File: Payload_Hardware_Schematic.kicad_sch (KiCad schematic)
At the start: 11 parts, among them J1 Micro_SD_Card, J2 Conn_01x06_Pin_5V, J3 Conn_01x06_Pin_3V3, J4 Conn_01x04_Pin, J5 Conn_01x08_Pin, U1 STM32F411 BlackPill, U2 MPM3610, U3 BMP388, U4 LSM9DS1, U5 MPM3610

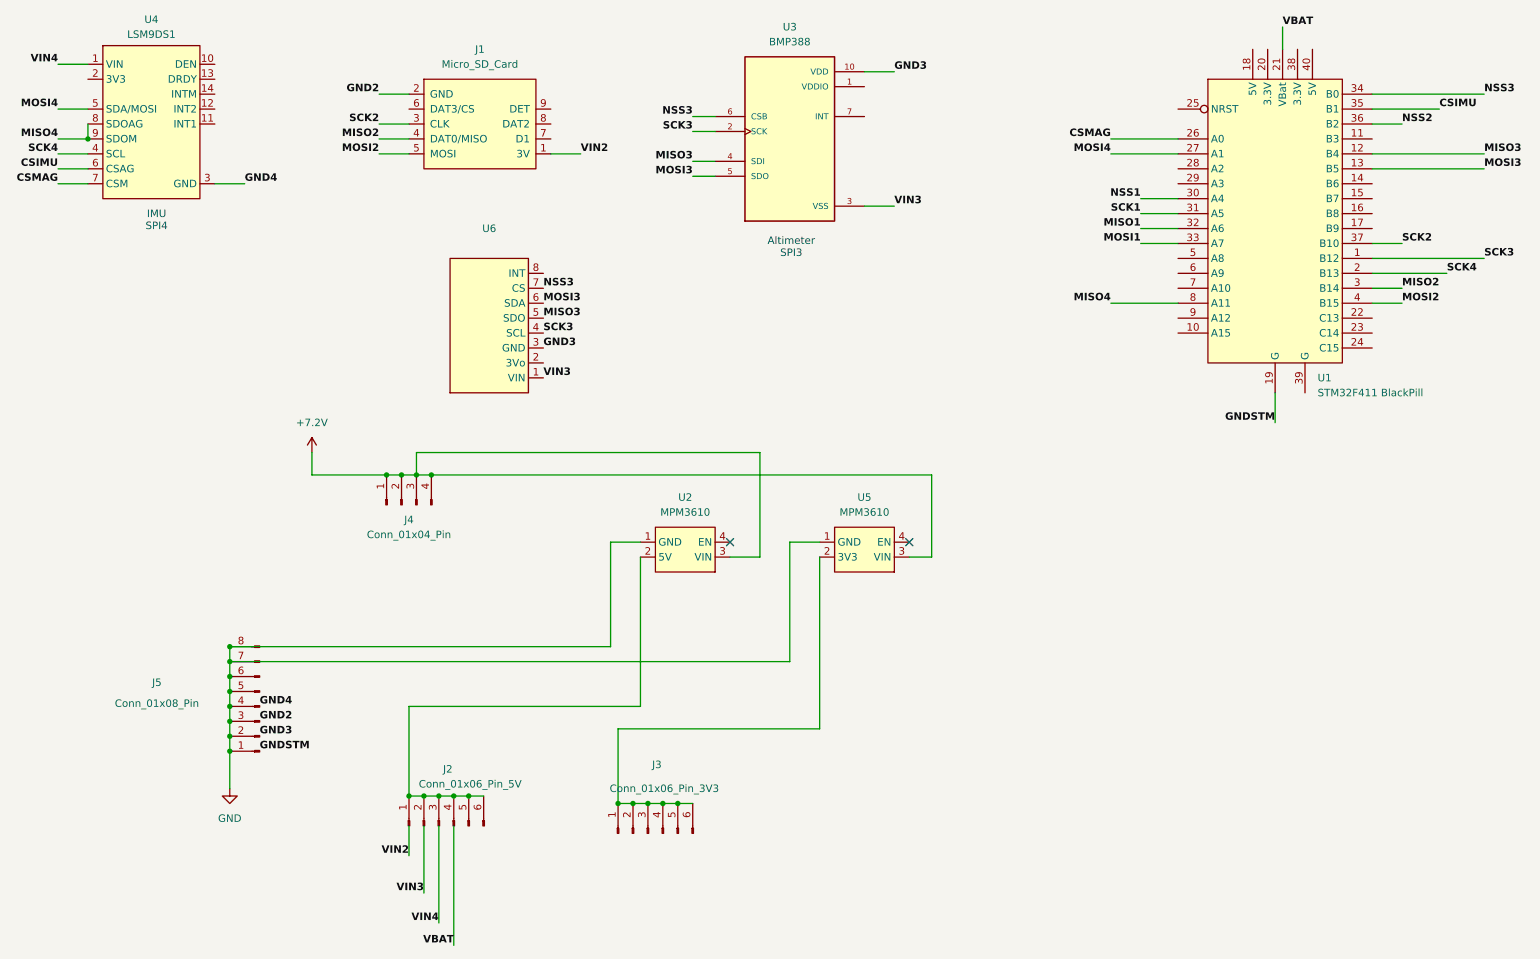
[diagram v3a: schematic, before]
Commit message: Fixed footprints and schematics
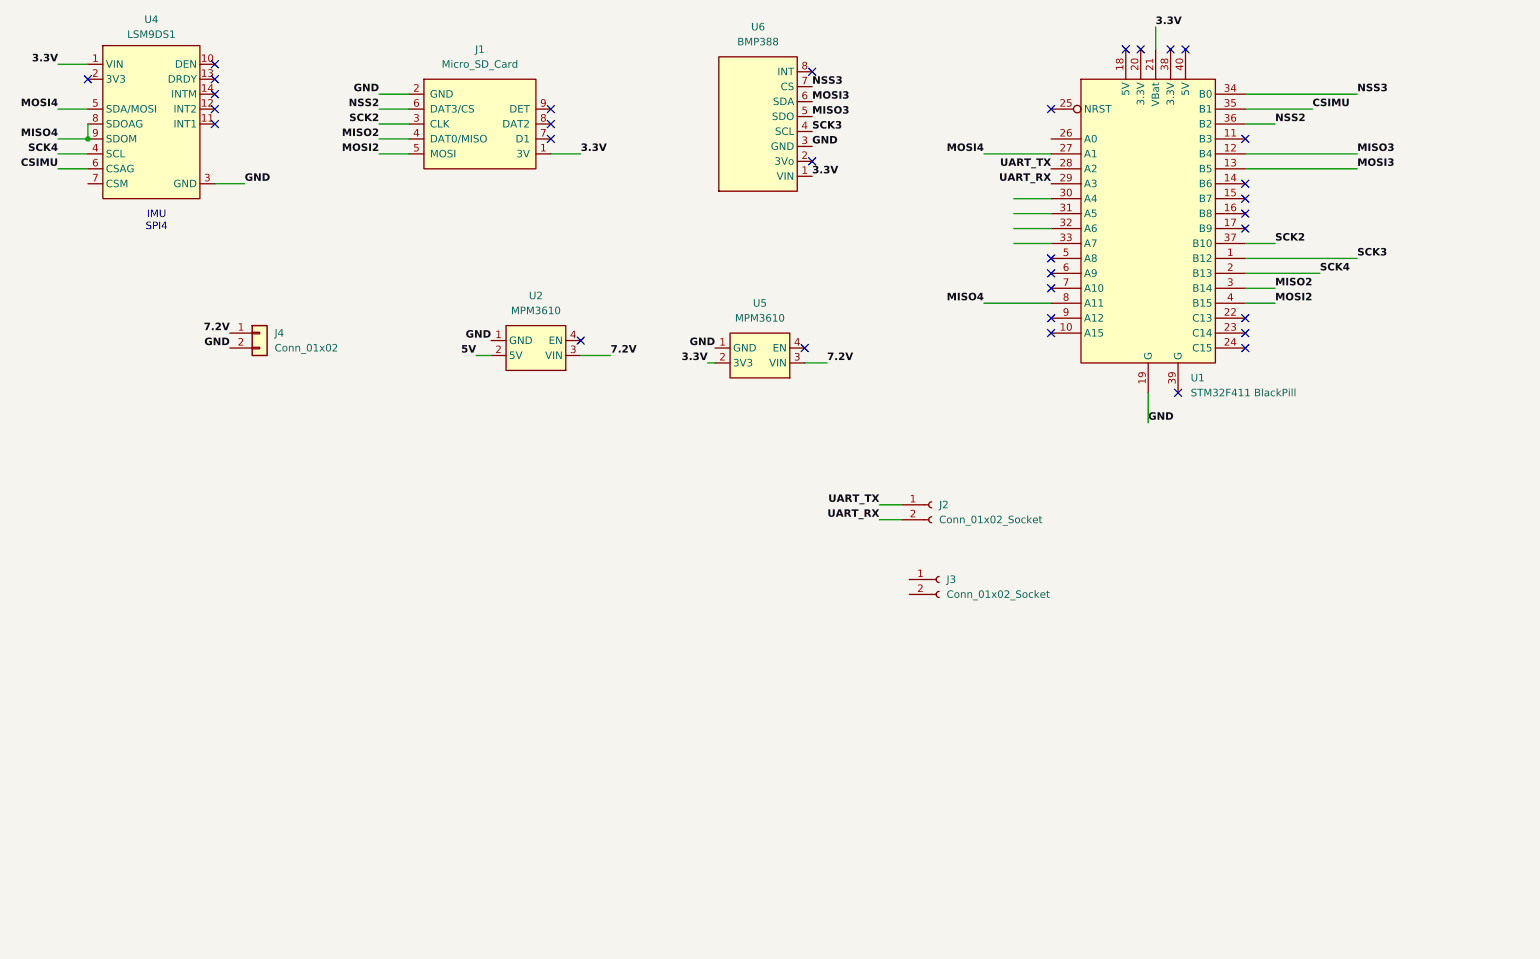
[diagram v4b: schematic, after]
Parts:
- removed J2: Conn_01x06_Pin_5V, Connector_PinSocket_2.54mm:PinSocket_1x06_P2.54mm_Vertical, symbol Connector:Conn_01x06_Pin
- removed J3: Conn_01x06_Pin_3V3, Connector_PinSocket_2.54mm:PinSocket_1x06_P2.54mm_Vertical, symbol Connector:Conn_01x06_Pin
- removed J4: Conn_01x04_Pin, Connector_PinSocket_2.54mm:PinSocket_1x04_P2.54mm_Vertical, symbol Connector:Conn_01x04_Pin
- removed J5: Conn_01x08_Pin, Connector_PinSocket_2.54mm:PinSocket_1x08_P2.54mm_Vertical, symbol Connector:Conn_01x08_Pin
- removed U3: BMP388, BMP388:BMP388_Breakout, symbol BMP388:BMP388
- added J2, J3: Conn_01x02_Socket, symbol Connector:Conn_01x02_Socket
- added J4: Conn_01x02, symbol Connector_Generic:Conn_01x02
- U6: value ~ -> BMP388
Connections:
- net GND3 is gone; now on net GND: U6.3 (GND)
- net GND4 is gone; now on net GND: U4.3 (GND)
- net GNDSTM is gone; now on net GND: U1.19 (G)
- net VBAT is gone; now on net GND: U1.21 (VBat)
- net VIN4 is gone; now on net GND: U4.1 (VIN)
- net VSS is gone; now on net GND: U6.1 (VIN)
- net GND: now also J1.2 (GND), U5.2 (3V3), J4.2 (Pin_2)
- net NSS2: now also J1.6 (DAT3/CS)
- net 5V: now reaches U2.2 (5V)
- net UART_TX: now reaches U1.28 (A2)
- net UART_TX: now also J2.1 (Pin_1)
- net UART_RX: now reaches U1.29 (A3)
- net UART_RX: now also J2.2 (Pin_2)
- net +7.2V renamed 7.2V
- net 7.2V: now also J4.1 (Pin_1)
- net CSMAG: no longer names the net of U4.7 (CSM)
- net CSMAG: no longer U1.26 (A0)
- net MISO1: no longer names the net of U1.32 (A6)
- net MOSI1: no longer names the net of U1.33 (A7)
- net NSS1: no longer names the net of U1.30 (A4)
- net SCK1: no longer names the net of U1.31 (A5)
- no-connect marks 2 -> 32
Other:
- note removed: "Altimeter SPI3"
- moved on the sheet: U1, U2, U5, U6

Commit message: updated footprints
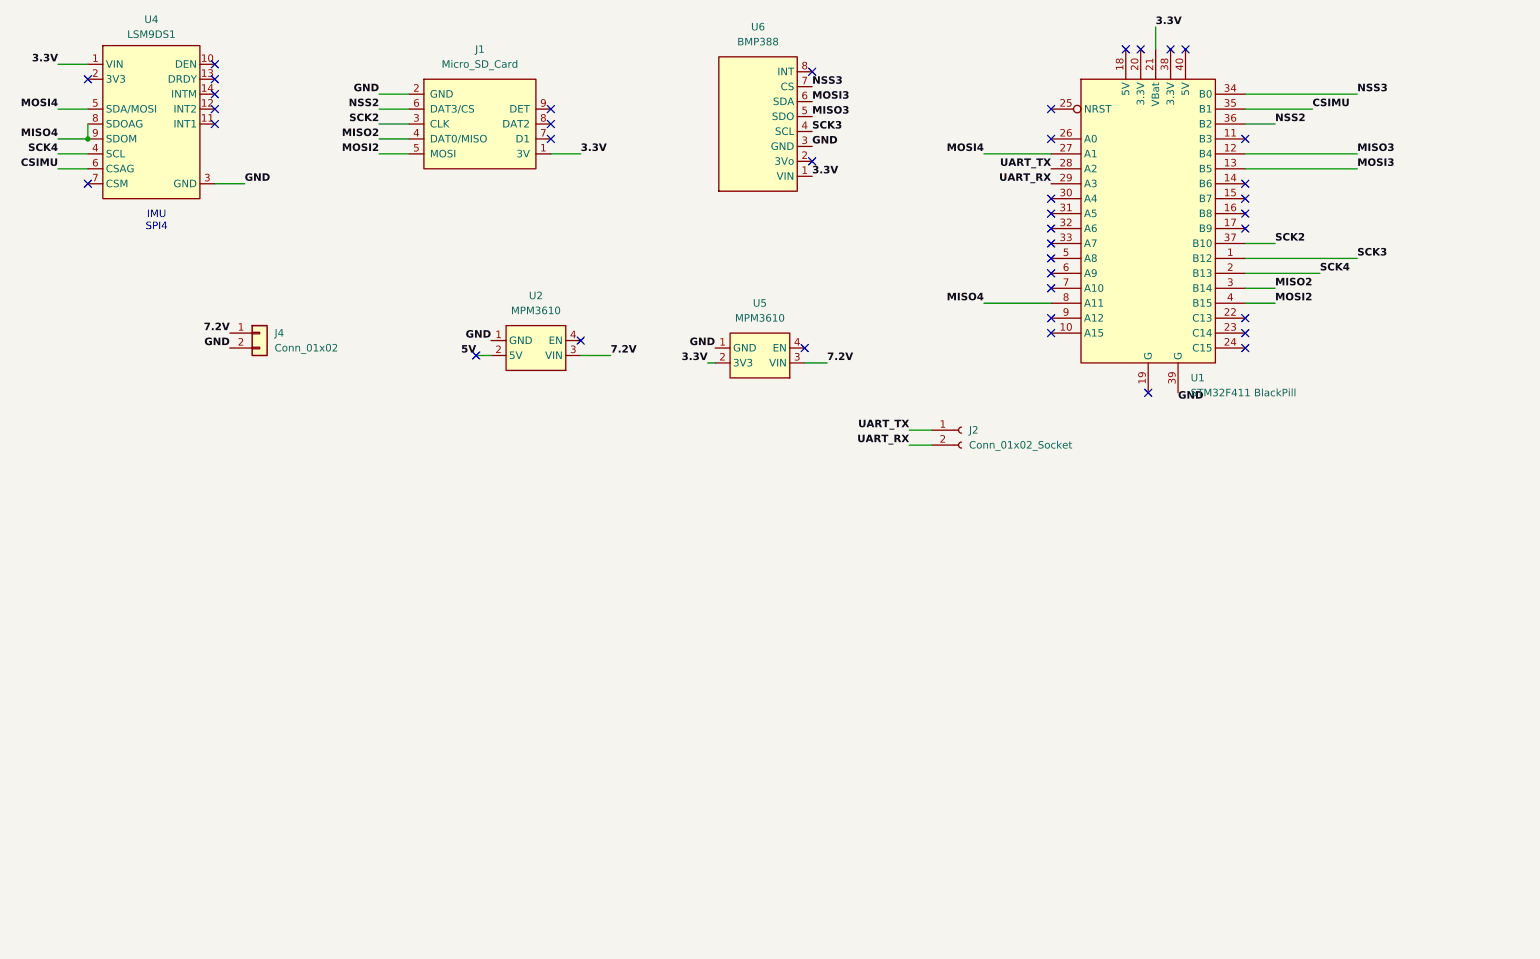
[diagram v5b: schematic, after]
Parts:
- removed J3: Conn_01x02_Socket, symbol Connector:Conn_01x02_Socket
- J2: footprint (none) -> Connector_PinSocket_2.54mm:PinSocket_1x02_P2.54mm_Vertical
- J4: footprint (none) -> Microfit-Header:CONN_SD-43650-001_02_MOL
- U2, U5: footprint PowerRegulation:MPM3610 -> PowerRugulators:MPM3610
- U6: footprint BMP388:BMP388_Breakout -> Payload-BMP388:BMP388_Breakout
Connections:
- net GND: now also U1.39 (G); no longer U1.19 (G)
- no-connect marks 32 -> 39
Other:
- moved on the sheet: J2
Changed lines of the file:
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@@
+	)
+	(no_connect
+		(at 34.29 46.99)
 	)
 	(no_connect
@@
 	)
 	(no_connect
-		(at 219.71 82.55)
+		(at 198.12 39.37)
+	)
+	(no_connect
+		(at 214.63 82.55)
 	)
 	(no_connect
@@
 	)
 	(no_connect
+		(at 198.12 57.15)
+	)
+	(no_connect
 		(at 198.12 59.69)
 	)
@@
 	)
 	(no_connect
+		(at 198.12 52.07)
+	)
+	(no_connect
 		(at 55.88 29.21)
 	)
@@
 	)
 	(no_connect
+		(at 198.12 49.53)
+	)
+	(no_connect
+		(at 198.12 54.61)
+	)
+	(no_connect
 		(at 156.21 74.93)
 	)
@@
 	)
 	(no_connect
+		(at 100.33 76.2)
+	)
+	(no_connect
 		(at 231.14 54.61)
 	)
@@
 	(wire
 		(pts
-			(xy 168.91 101.6) (xy 172.72 101.6)
-		)
-		(stroke
-			(width 0)
-			(type default)
-		)
-	)
-	(wire
-		(pts
-			(xy 191.77 57.15) (xy 198.12 57.15)
+			(xy 173.99 88.9) (xy 177.8 88.9)
 		)
 		(stroke
@@
 	(wire
 		(pts
-			(xy 191.77 52.07) (xy 198.12 52.07)
-		)
-		(stroke
-			(width 0)
-			(type default)
-		)
-	)
-	(wire
-		(pts
 			(xy 231.14 36.83) (xy 236.22 36.83)
 		)
@@
 	(wire
 		(pts
-			(xy 191.77 54.61) (xy 198.12 54.61)
-		)
-		(stroke
-			(width 0)
-			(type default)
-		)
-	)
-	(wire
-		(pts
 			(xy 29.21 39.37) (xy 34.29 39.37)
 		)
@@
 	(wire
 		(pts
-			(xy 214.63 82.55) (xy 214.63 87.63)
-		)
-		(stroke
-			(width 0)
-			(type default)
-		)
-	)
-	(wire
-		(pts
 			(xy 83.82 31.75) (xy 88.9 31.75)
 		)
@@
 	(wire
 		(pts
-			(xy 191.77 49.53) (xy 198.12 49.53)
-		)
-		(stroke
-			(width 0)
-			(type default)
-		)
-	)
-	(wire
-		(pts
 			(xy 231.14 41.91) (xy 250.19 41.91)
 		)
@@
 	(wire
 		(pts
-			(xy 168.91 104.14) (xy 172.72 104.14)
+			(xy 173.99 91.44) (xy 177.8 91.44)
 		)
 		(stroke
@@
 	)
 	(label "GND"
-		(at 214.63 87.63 0)
-		(effects
-			(font
-				(size 1.27 1.27)
-				(thickness 0.254)
-				(bold yes)
-			)
-			(justify left bottom)
+		(at 219.71 82.55 0)
+		(effects
+			(font
+				(size 1.27 1.27)
+				(thickness 0.254)
+				(bold yes)
+			)
+			(justify top)
 		)
 	)
@@
 	)
 	(label "UART_RX"
-		(at 168.91 104.14 180)
+		(at 173.99 91.44 180)
 		(effects
 			(font
@@
 	)
 	(label "UART_TX"
-		(at 168.91 101.6 180)
+		(at 173.99 88.9 180)
 		(effects
 			(font
@@
 			)
 			(justify left bottom)
-		)
-	)
-	(symbol
-		(lib_id "Connector:Conn_01x02_Socket")
-		(at 179.07 114.3 0)
-		(unit 1)
-		(exclude_from_sim no)
-		(in_bom yes)
-		(on_board yes)
-		(dnp no)
-		(fields_autoplaced yes)
-		(property "Reference" "J3"
-			(at 180.34 114.2999 0)
-			(effects
-				(font
-					(size 1.27 1.27)
-				)
-				(justify left)
-			)
-		)
-		(property "Value" "Conn_01x02_Socket"
-			(at 180.34 116.8399 0)
-			(effects
-				(font
-					(size 1.27 1.27)
-				)
-				(justify left)
-			)
-		)
-		(property "Footprint" ""
-			(at 179.07 114.3 0)
-			(effects
-				(font
-					(size 1.27 1.27)
-				)
-				(hide yes)
-			)
-		)
-		(property "Datasheet" "~"
-			(at 179.07 114.3 0)
-			(effects
-				(font
-					(size 1.27 1.27)
-				)
-				(hide yes)
-			)
-		)
-		(property "Description" "Generic connector, single row, 01x02, script generated"
-			(at 179.07 114.3 0)
-			(effects
-				(font
-					(size 1.27 1.27)
-				)
-				(hide yes)
-			)
-		)
-		(pin "2"
-		)
-		(pin "1"
-		)
-		(instances
-			(project "Payload_Hardware_Schematic"
-				(path "/f4ead8bb-2437-4e54-a6d9-f5ca11bfd675"
-					(reference "J3")
-					(unit 1)
-				)
-			)
 		)
 	)
@@
 			)
 		)
-		(property "Footprint" "BMP388:BMP388_Breakout"
+		(property "Footprint" "Payload-BMP388:BMP388_Breakout"
 			(at 151.13 34.29 0)
 			(effects
@@
 			)
 		)
-		(property "Footprint" ""
+		(property "Footprint" "Microfit-Header:CONN_SD-43650-001_02_MOL"
 			(at 63.5 72.39 0)
 			(effects
@@
 			)
 		)
-		(property "Footprint" "PowerRegulation:MPM3610"
+		(property "Footprint" "PowerRugulators:MPM3610"
 			(at 147.32 69.85 0)
 			(effects
@@
 			)
 		)
-		(property "Footprint" "PowerRegulation:MPM3610"
+		(property "Footprint" "PowerRugulators:MPM3610"
 			(at 109.22 68.58 0)
 			(effects
@@
 	(symbol
 		(lib_id "Connector:Conn_01x02_Socket")
-		(at 177.8 101.6 0)
+		(at 182.88 88.9 0)
 		(unit 1)
 		(exclude_from_sim no)
@@
 		(fields_autoplaced yes)
 		(property "Reference" "J2"
-			(at 179.07 101.5999 0)
+			(at 184.15 88.8999 0)
 			(effects
 				(font
@@
 		)
 		(property "Value" "Conn_01x02_Socket"
-			(at 179.07 104.1399 0)
+			(at 184.15 91.4399 0)
 			(effects
 				(font
@@
 			)
 		)
-		(property "Footprint" ""
-			(at 177.8 101.6 0)
+		(property "Footprint" "Connector_PinSocket_2.54mm:PinSocket_1x02_P2.54mm_Vertical"
+			(at 182.88 88.9 0)
 			(effects
 				(font
@@
 		)
 		(property "Datasheet" "~"
-			(at 177.8 101.6 0)
+			(at 182.88 88.9 0)
 			(effects
 				(font
@@
 		)
 		(property "Description" "Generic connector, single row, 01x02, script generated"
-			(at 177.8 101.6 0)
-			(effects
-				(font
+			(at 182.88 88.9 0)
+			(effects
+				(font

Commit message: fixed errors and schematic updates
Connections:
- net GND: no longer J1.1 (3V), J1.G1 (GND), J1.G2 (GND), J1.G3 (GND), J1.G4 (GND), U1.21 (VBat), U4.1 (VIN), U5.2 (3V3), U6.1 (VIN)
- new net: J1.1 (3V), U1.21 (VBat), U4.1 (VIN), U5.2 (3V3), U6.1 (VIN)
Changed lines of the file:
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@@
 	)
 	(junction
-		(at 34.29 39.37)
+		(at 31.75 39.37)
 		(diameter 0)
 		(color 0 0 0 0)
@@
 	(wire
 		(pts
+			(xy 29.21 39.37) (xy 31.75 39.37)
+		)
+		(stroke
+			(width 0)
+			(type default)
+		)
+	)
+	(wire
+		(pts
 			(xy 231.14 57.15) (xy 236.22 57.15)
 		)
@@
 	(wire
 		(pts
-			(xy 29.21 39.37) (xy 34.29 39.37)
-		)
-		(stroke
-			(width 0)
-			(type default)
-		)
-	)
-	(wire
-		(pts
 			(xy 139.7 77.47) (xy 140.97 77.47)
 		)
@@
 	(wire
 		(pts
+			(xy 31.75 39.37) (xy 34.29 39.37)
+		)
+		(stroke
+			(width 0)
+			(type default)
+		)
+	)
+	(wire
+		(pts
 			(xy 198.12 67.31) (xy 186.69 67.31)
 		)
@@
 	(wire
 		(pts
-			(xy 113.03 41.91) (xy 118.11 41.91)
-		)
-		(stroke
-			(width 0)
-			(type default)
-		)
-	)
-	(wire
-		(pts
-			(xy 34.29 36.83) (xy 34.29 39.37)
-		)
-		(stroke
-			(width 0)
-			(type default)
-		)
-	)
-	(wire
-		(pts
 			(xy 83.82 39.37) (xy 88.9 39.37)
 		)
@@
 	(wire
 		(pts
-			(xy 83.82 31.75) (xy 88.9 31.75)
-		)
-		(stroke
-			(width 0)
-			(type default)
-		)
-	)
-	(wire
-		(pts
 			(xy 231.14 41.91) (xy 250.19 41.91)
 		)
@@
 	(wire
 		(pts
+			(xy 31.75 39.37) (xy 31.75 36.83)
+		)
+		(stroke
+			(width 0)
+			(type default)
+		)
+	)
+	(wire
+		(pts
 			(xy 156.21 77.47) (xy 160.02 77.47)
 		)
@@
 		(pts
 			(xy 118.11 76.2) (xy 123.19 76.2)
+		)
+		(stroke
+			(width 0)
+			(type default)
+		)
+	)
+	(wire
+		(pts
+			(xy 31.75 36.83) (xy 34.29 36.83)
 		)
 		(stroke
@@
 		)
 	)
+	(label "7.2V"
+		(at 123.19 76.2 0)
+		(effects
+			(font
+				(size 1.27 1.27)
+				(thickness 0.254)
+				(bold yes)
+				(color 0 0 0 1)
+			)
+			(justify left bottom)
+		)
+	)
 	(label "NSS2"
 		(at 236.22 36.83 0)
@@
 		)
 	)
-	(label "7.2V"
-		(at 123.19 76.2 0)
-		(effects
-			(font
-				(size 1.27 1.27)
-				(thickness 0.254)
-				(bold yes)
-				(color 0 0 0 1)
-			)
-			(justify left bottom)
-		)
-	)
 	(label "UART_RX"
 		(at 198.12 46.99 180)
@@
 	)
 	(label "GND"
-		(at 83.82 31.75 180)
-		(effects
-			(font
-				(size 1.27 1.27)
-				(thickness 0.254)
-				(bold yes)
-			)
-			(justify right bottom)
+		(at 113.03 41.91 0)
+		(effects
+			(font
+				(size 1.27 1.27)
+				(thickness 0.254)
+				(bold yes)
+			)
+			(justify left bottom)
 		)
 	)
@@
 	)
 	(label "3.3V"
-		(at 118.11 41.91 0)
+		(at 88.9 31.75 180)
 		(effects
 			(font
@@
 				(color 255 0 0 1)
 			)
-			(justify left bottom)
+			(justify right bottom)
 		)
 	)
@@
 		(pin "4"
 		)
-		(pin "G1"
-		)
-		(pin "G2"
-		)
-		(pin "G3"
-		)
-		(pin "G4"
-		)
 		(pin "2"
